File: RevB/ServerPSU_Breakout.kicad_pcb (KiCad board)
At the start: 2 copper layers, 124 x 83.9 mm, 78 parts, among them J1 Conn_01x05, J2 Conn_01x14, J3 Conn_01x01, J4 Conn_01x01, Q1 DMG2302U, SW1 SW_DIP_x03, SW2 SW_SPDT, SW3 SW_DIP_x03, U1 LMR14206, U2 STM32F072RBTx, U3 4051, U4 MIC1555-YM5, U5 4066, U6 MCP1415, U7 AZ1117CR-3.3

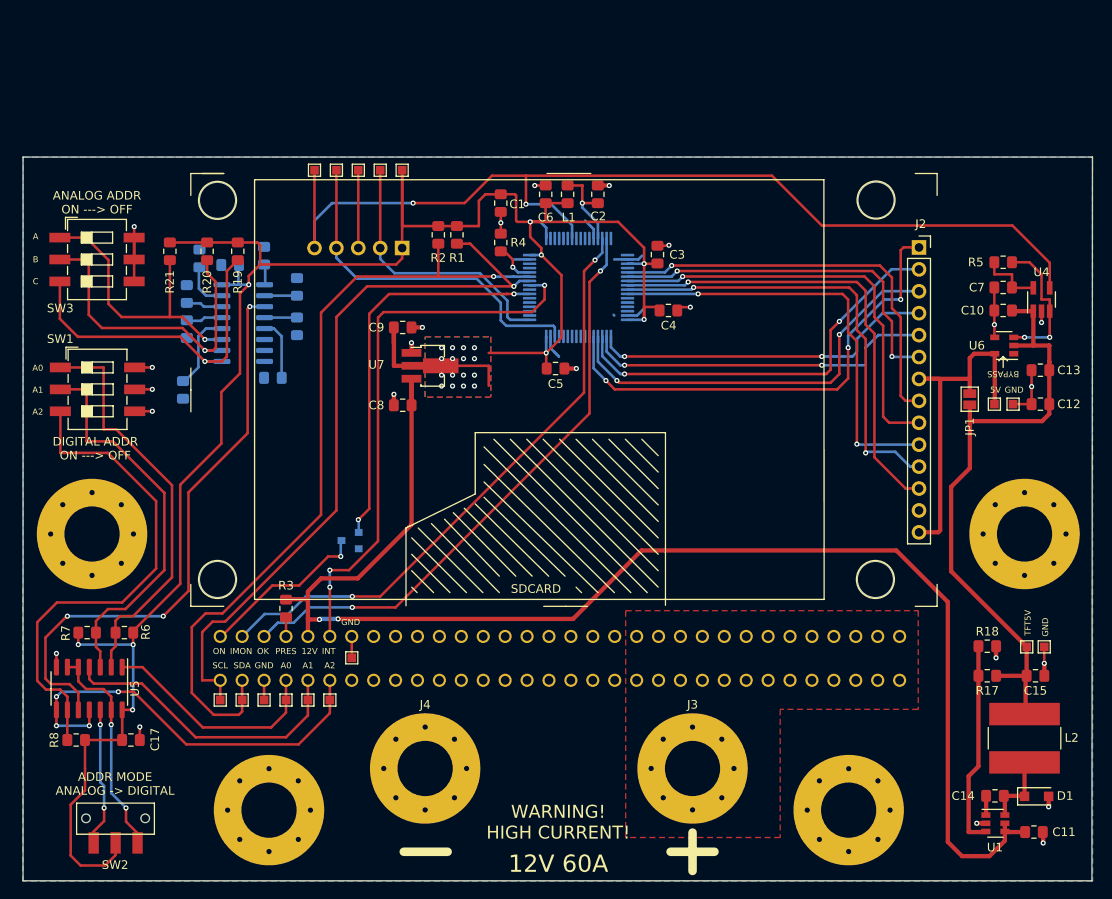
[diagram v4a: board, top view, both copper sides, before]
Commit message: hw update
updated revb. Added board connectors for device stacking
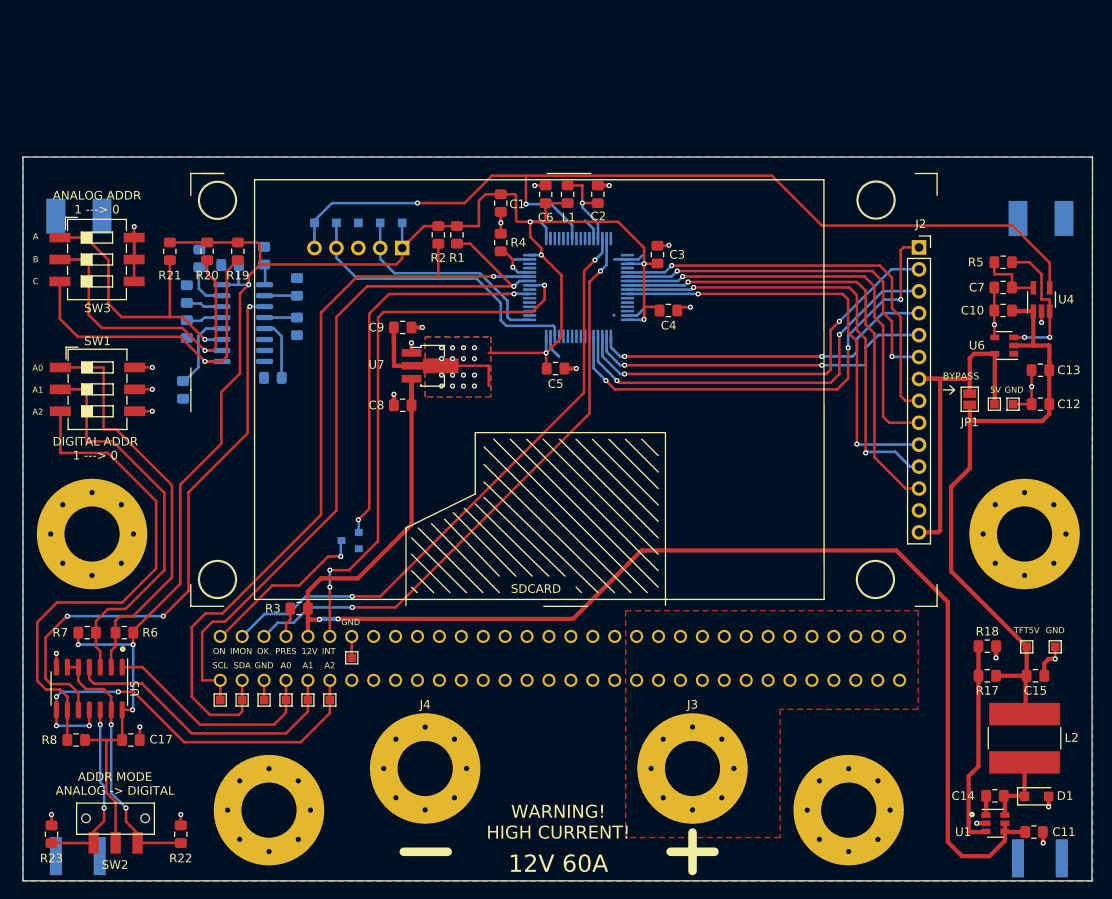
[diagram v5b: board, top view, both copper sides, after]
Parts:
- added R22: 220R, Resistor_SMD:R_0805_2012Metric_Pad1.15x1.40mm_HandSolder, F.Cu at (117.7, 137.7)
- added R23: 220R, Resistor_SMD:R_0805_2012Metric_Pad1.15x1.40mm_HandSolder, F.Cu at (102.7, 137.7)
- added REF**: TermiMate_505072_1_Way_1_Row_Right_Angle_PCB_Socket_SMD, TermiMate One-Circuit Terminal-Style Connector System:TermiMate_505072_1_Way_1_Row_Right_Angle_PCB_Socket_SMD, B.Cu at (220.1, 66.3)
- added REF**: TermiMate_505071_1_Way_1_Row_Right_Angle_PCB_Header_SMD, TermiMate One-Circuit Terminal-Style Connector System:TermiMate_505071_1_Way_1_Row_Right_Angle_PCB_Header, B.Cu at (214.8, 140.5)
- added REF**: TermiMate_505071_1_Way_1_Row_Right_Angle_PCB_Header_SMD, TermiMate One-Circuit Terminal-Style Connector System:TermiMate_505071_1_Way_1_Row_Right_Angle_PCB_Header, B.Cu at (219.8, 140.5)
- added REF**: TermiMate_505072_1_Way_1_Row_Right_Angle_PCB_Socket_SMD, TermiMate One-Circuit Terminal-Style Connector System:TermiMate_505072_1_Way_1_Row_Right_Angle_PCB_Socket_SMD, B.Cu at (214.8, 66.3)
- added REF**: TermiMate_505072_1_Way_1_Row_Right_Angle_PCB_Socket_SMD, TermiMate One-Circuit Terminal-Style Connector System:TermiMate_505072_1_Way_1_Row_Right_Angle_PCB_Socket_SMD, B.Cu at (108.6, 66.0)
- added REF**: TermiMate_505072_1_Way_1_Row_Right_Angle_PCB_Socket_SMD, TermiMate One-Circuit Terminal-Style Connector System:TermiMate_505072_1_Way_1_Row_Right_Angle_PCB_Socket_SMD, B.Cu at (103.3, 66.0)
- added REF**: TermiMate_505071_1_Way_1_Row_Right_Angle_PCB_Header_SMD, TermiMate One-Circuit Terminal-Style Connector System:TermiMate_505071_1_Way_1_Row_Right_Angle_PCB_Header, B.Cu at (108.3, 140.2)
- added REF**: TermiMate_505071_1_Way_1_Row_Right_Angle_PCB_Header_SMD, TermiMate One-Circuit Terminal-Style Connector System:TermiMate_505071_1_Way_1_Row_Right_Angle_PCB_Header, B.Cu at (103.3, 140.2)
- J1: footprint Connector_PinHeader_2.54mm:PinHeader_1x05_P2.54mm_Horizontal -> Connector_PinHeader_2.54mm:PinHeader_1x05_P2.54mm_Vertical
- TP1, TP2, TP22, TP23, TP9: moved to B.Cu
- moved TP1 6.10 mm to (143.4, 66.8), turned to 90 degrees
- moved TP2 6.10 mm to (138.3, 66.8), turned to 90 degrees
- moved TP22 6.10 mm to (140.8, 66.8), turned to 90 degrees
- moved TP23 6.10 mm to (135.8, 66.8), turned to 90 degrees
- moved TP9 6.10 mm to (133.2, 66.8)
- moved R3 1.52 mm to (131.4, 111.5), turned to 0 degrees
- moved TP6 1.27 mm to (219.1, 116.0)
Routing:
- net /HighVoltageControl/MCU_3V3: track 259.6 -> 238.3 mm
- net /MCU/NRST: track 117.9 -> 108.8 mm
- net /MCU/SWDIO: track 41.1 -> 34.5 mm
- net /MCU/SWCLK: track 31.6 -> 25.0 mm
- net GNDS: track 79.8 -> 74.3 mm, vias 23 -> 25
- net /MCU/SMBUS_Addressing/ENABLE_DIGITAL: track 25.7 -> 30.7 mm
- net /MCU/SMBUS_Addressing/ENABLE_ANALOG: track 16.1 -> 21.0 mm
- net /HighVoltageControl/PSU_12VSB: track 163.0 -> 160.4 mm
- net /HighVoltageControl/PSU_PRES: track 2.21 -> 3.19 mm
- net /PSUConnector/PSU_ADDR1: track 34.6 -> 34.0 mm
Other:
- board text added: "3V3"
- board text added: "A B C ADDR 0 0 0 80/88 1 0 0 81/89 0 1 0 82/90 1 1 0 83/91 0 0 1 84/92 1 0 1 85/93 0 1 1 86/94 1 1 1 97/95"
- board text added: "A B C ADDR 0 0 0 B0/A0 1 0 0 B2/A2 0 1 0 B4/A4 1 1 0 B6/A6 0 0 1 B8/A8 1 0 1 BA/AA 0 1 1 BC/AC 1 1 1 BE/AE"
- board text added: "ANALOG ADDR 1 ---> 0"
- board text added: "ANALOG SETTINGS: ----------"
- board text added: "CLK"
- board text added: "DIGITAL ADDR 1 ---> 0"
- board text added: "DIGITAL SETTINGS: ----------"
- board text added: "IO"
- board text added: "RST"
- board text removed: "ANALOG ADDR ON ---> OFF"
- board text removed: "DIGITAL ADDR ON ---> OFF"

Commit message: hw update
revb layout completed
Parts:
- removed the REF** at (220.1, 66.3)
- removed the REF** at (214.8, 140.5)
- removed the REF** at (219.8, 140.5)
- removed the REF** at (214.8, 66.3)
- removed the REF** at (108.6, 66.0)
- removed the REF** at (103.3, 66.0)
- removed the REF** at (108.3, 140.2)
- removed the REF** at (103.3, 140.2)
- C17, R6, R7, R8, U5: moved to B.Cu
- SW2: footprint JS_Series_Sub-Miniature_Slide_Switches:JS102011SAQN -> Connector_PinHeader_2.54mm:PinHeader_1x03_P2.54mm_Vertical
- moved C17 40.8 mm to (127.0, 88.8), turned to 90 degrees
- moved R8 40.8 mm to (120.7, 88.8), turned to 270 degrees
- moved U5 30.4 mm to (123.2, 94.9), turned to 90 degrees
- moved TP8 23.6 mm to (207.6, 65.2), turned to 90 degrees
- moved R7 21.3 mm to (124.5, 102.2), turned to 90 degrees
- moved R6 20.2 mm to (127.4, 102.2), turned to 90 degrees
- moved SW2 19.8 mm to (110.6, 117.6), turned to 270 degrees
- moved TP7 18.7 mm to (207.6, 69.6), turned to 90 degrees
- moved SW1 17.1 mm to (108.1, 103.3)
- moved REF** 16.3 mm to (215.2, 86.6)
- moved REF** 16.3 mm to (107.4, 86.6)
- moved R22 16.2 mm to (110.5, 123.2), turned to 270 degrees
- moved R23 14.7 mm to (105.4, 123.2), turned to 270 degrees
- moved C14 14.0 mm to (212.0, 119.2)
- moved L2 14.0 mm to (215.5, 112.5)
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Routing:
- net Net-(U3-Pad3): track 67.6 -> 21.5 mm, vias 3 -> 2
- net /MCU/SMBUS_Addressing/ENABLE_ANALOG: track 21.0 -> 50.2 mm
- net /PSUConnector/PSU_ADDR0: track 26.1 -> 51.4 mm, vias 0 -> 1
- net Net-(R8-Pad2): track 58.5 -> 34.6 mm, vias 0 -> 1
- net /PSUConnector/PSU_ADDR1: track 34.0 -> 52.2 mm, vias 0 -> 1
- net /PSUConnector/PSU_ADDR2: track 48.6 -> 65.4 mm, vias 4 -> 1
- net Net-(R6-Pad2): track 47.7 -> 31.9 mm, vias 0 -> 1
- net Net-(R7-Pad2): track 45.4 -> 30.3 mm, vias 0 -> 1
- net /HighVoltageControl/MCU_3V3: track 238.3 -> 252.5 mm, vias 25 -> 26
- net /HighVoltageControl/PSU_12VSB: track 160.4 -> 146.7 mm
- net /MCU/SMBUS_Addressing/ENABLE_DIGITAL: track 30.7 -> 38.5 mm
- net /MCU/TFT_DelayedReset/TFT_VDD_OUT: track 41.4 -> 46.2 mm
- net /MCU/NRST: track 108.8 -> 105.8 mm
- net /MCU/TFTRST_5V: track 71.9 -> 73.9 mm
- net GNDS: track 74.3 -> 72.7 mm, vias 25 -> 24
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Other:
- board text added: "ANALOG ADDR 1 <--> 0"
- board text added: "BYPASS NRST TIMER --->"
- board text added: "DIGITAL ADDR 1 <--> 0"
- board text added: "RevB 3220 C.Sutton"
- board text removed: "ANALOG ADDR 1 ---> 0"
- board text removed: "BYPASS"
- board text removed: "DIGITAL ADDR 1 ---> 0"
- board text removed: "RevB"
